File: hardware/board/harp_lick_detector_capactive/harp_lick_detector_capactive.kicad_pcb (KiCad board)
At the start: 4 copper layers, 62.5 x 60.5 mm, 117 parts, among them J1 USB_C_Receptacle_USB2.0, J10 Conn_01x02_Male, J2 Conn_01x03_Male, J3 Conn_01x03_Male, J4 AudioJack3, J5 Barrel_Jack_Switch, J6 Conn_Coaxial, J7 Conn_Coaxial, J8 Conn_Coaxial, J9 Conn_Coaxial, U1 RP2040, U10 LTC6263, U11 CD74AC04, U2 W25Q128JVS, U3 ADUM4160, U4 TPD2EUSB30, U5 LT3030, U6 LM27762, U7 AD9833xRM, U8 LTC6263, U9 LTC6268xS6-10, X1 ECS-TXO-2016, X2 ASE-25.000MHZ-L-C-T

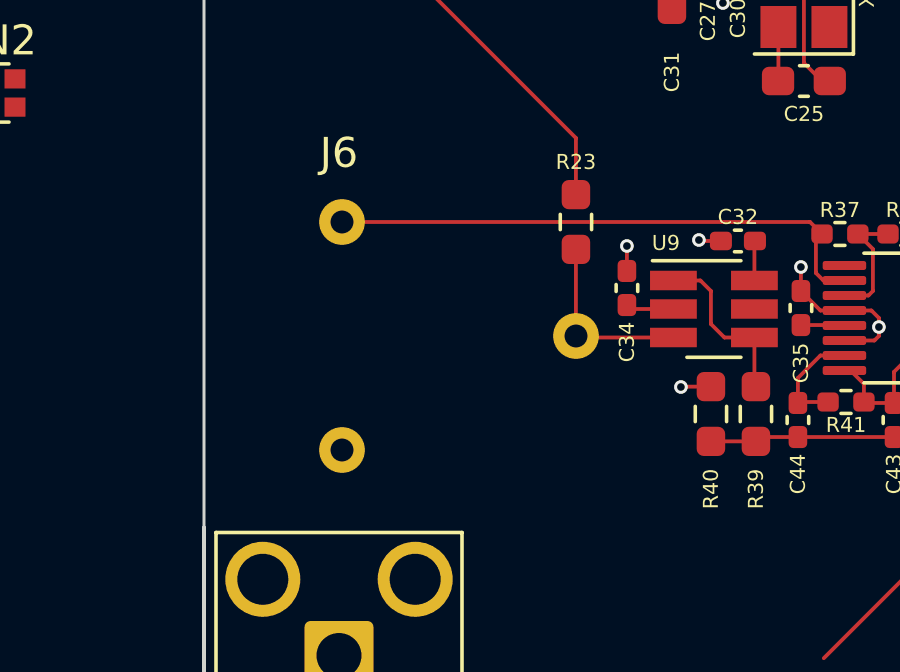
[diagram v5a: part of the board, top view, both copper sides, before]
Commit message: update bandpass filter; plan pico shield version
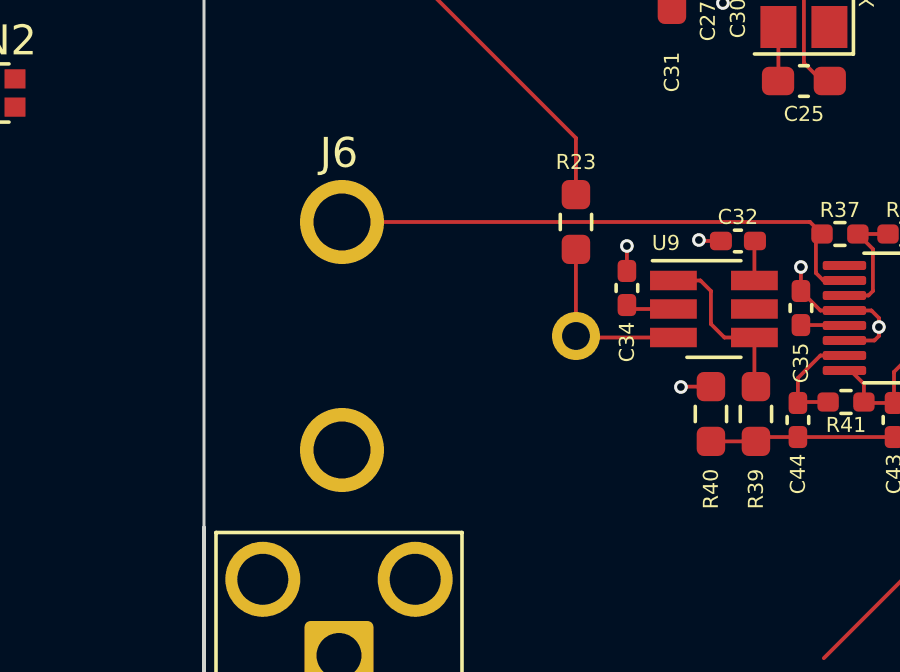
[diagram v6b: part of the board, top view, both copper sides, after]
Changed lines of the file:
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@@
     )
     (fp_line (start -4.825 17.6) (end -4.826 4.6) (layer "Dwgs.User") (width 0.12))
-    (fp_line (start -4.825 17.6) (end 4.825 17.6) (layer "Dwgs.User") (width 0.12))
     (fp_line (start -4.8255 -4.2) (end 4.8255 -4.2) (layer "Dwgs.User") (width 0.12))
     (fp_line (start -4.826 4.6) (end 4.825 4.6) (layer "Dwgs.User") (width 0.12))
+    (fp_line (start -4.825 17.6) (end 4.825 17.6) (layer "Dwgs.User") (width 0.12))
     (fp_line (start 4.825 4.6) (end 4.825 17.6) (layer "Dwgs.User") (width 0.12))
+    (fp_line (start 5.33 -4.69) (end -5.33 -4.69) (layer "F.CrtYd") (width 0.05))
+    (fp_line (start 5.33 5.1) (end 5.33 -4.69) (layer "F.CrtYd") (width 0.05))
     (fp_line (start 5.33 5.1) (end -5.33 5.1) (layer "F.CrtYd") (width 0.05))
-    (fp_line (start 5.33 5.1) (end 5.33 -4.69) (layer "F.CrtYd") (width 0.05))
     (fp_line (start -5.33 5.1) (end -5.33 -4.69) (layer "F.CrtYd") (width 0.05))
-    (fp_line (start 5.33 -4.69) (end -5.33 -4.69) (layer "F.CrtYd") (width 0.05))
-    (pad "1" thru_hole circle (at 0 -7.8 270) (size 1.524 1.524) (drill 0.762) (layers *.Cu *.Mask)
+    (pad "1" thru_hole circle (at 0 -7.8 270) (size 1.6 1.6) (drill 0.93) (layers *.Cu *.Mask)
       (net 41 "Net-(J6-Pad1)") (pinfunction "In") (pintype "passive"))
-    (pad "2" thru_hole circle (at 3.8 0 270) (size 1.524 1.524) (drill 0.762) (layers *.Cu *.Mask)
+    (pad "2" thru_hole circle (at 3.8 0 270) (size 2.8 2.8) (drill 1.9) (layers *.Cu *.Mask)
       (net 42 "Net-(J6-Pad2)") (pinfunction "Ext") (pintype "passive"))
-    (pad "2" thru_hole circle (at -3.8 0 270) (size 1.524 1.524) (drill 0.762) (layers *.Cu *.Mask)
+    (pad "2" thru_hole circle (at -3.8 0 270) (size 2.8 2.8) (drill 1.9) (layers *.Cu *.Mask)
       (net 42 "Net-(J6-Pad2)") (pinfunction "Ext") (pintype "passive"))
   )

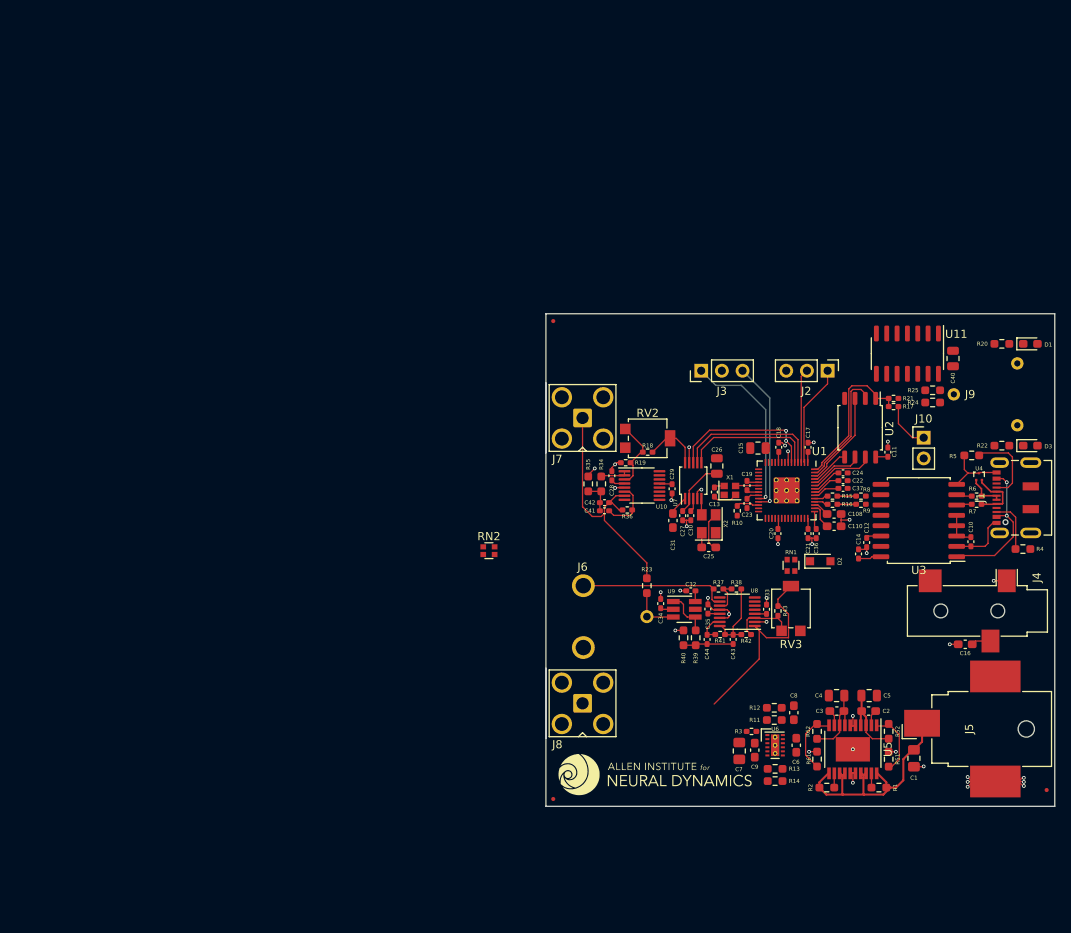
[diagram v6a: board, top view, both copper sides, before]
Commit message: draft ads7029 pio driver
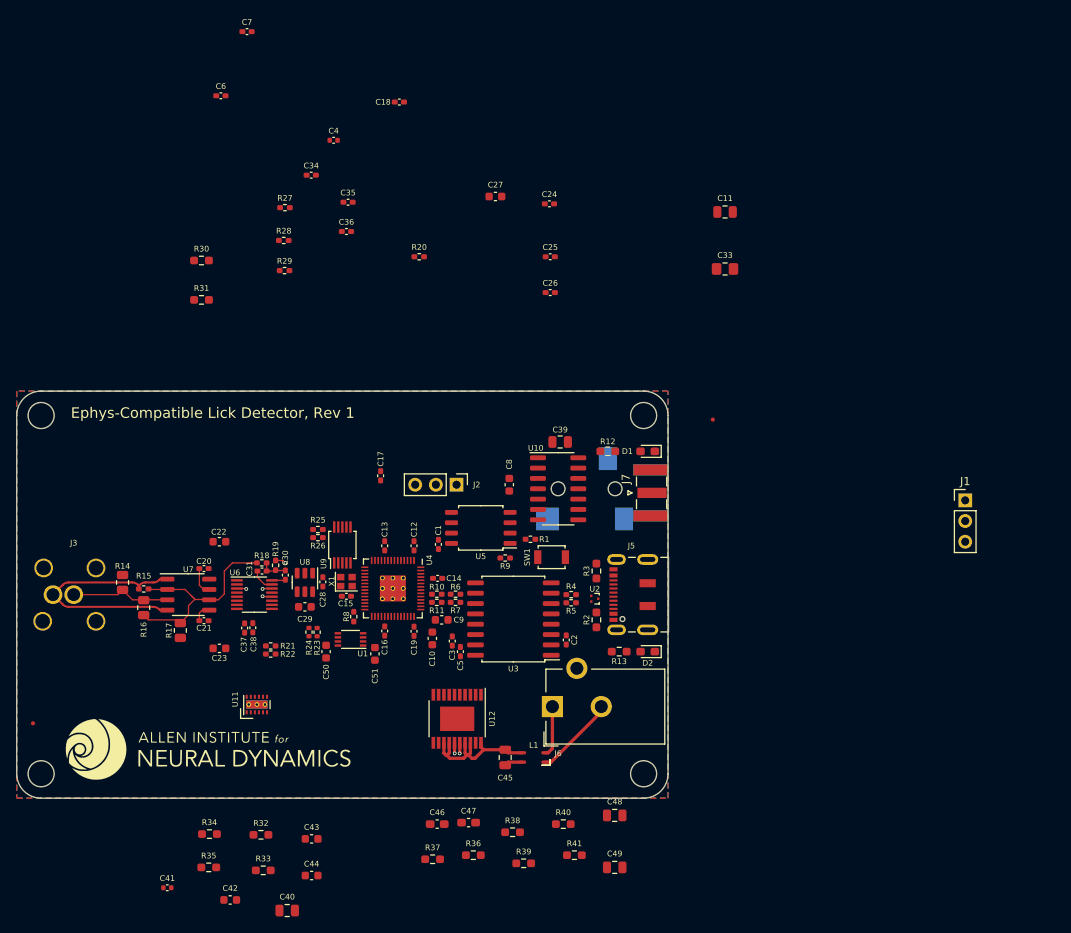
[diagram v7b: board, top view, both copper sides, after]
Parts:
- removed C108, C110: 1uF, Capacitor_SMD:C_0603_1608Metric_Pad1.08x0.95mm_HandSolder
- removed C32: 100nF, Capacitor_SMD:C_0402_1005Metric_Pad0.74x0.62mm_HandSolder
- removed D3: LED, LED_SMD:LED_0603_1608Metric_Pad1.05x0.95mm_HandSolder
- removed the G*** at (183.3, 115.2)
- removed J10: Conn_01x02_Male, Connector_PinHeader_2.54mm:PinHeader_1x02_P2.54mm_Vertical
- removed J8: Conn_Coaxial, Connector_Coaxial:SMA_Amphenol_901-143_Horizontal
- removed J9: Conn_Coaxial, machine_agency_components:conn_bnc_receptacle_50ohm
- removed R42, R43: 390, Resistor_SMD:R_0402_1005Metric_Pad0.72x0.64mm_HandSolder
- removed R51, R61: 100K, Resistor_SMD:R_0603_1608Metric_Pad0.98x0.95mm_HandSolder
- removed R52: 309K, Resistor_SMD:R_0603_1608Metric_Pad0.98x0.95mm_HandSolder
- removed R62: 172K, Resistor_SMD:R_0603_1608Metric_Pad0.98x0.95mm_HandSolder
- removed RN1, RN2: 5K, Resistor_SMD:R_Array_Convex_2x0606
- removed RV2, RV3: R_Potentiometer_Trim, Potentiometer_SMD:Potentiometer_Bourns_3314G_Vertical
- removed X2: ASE-25.000MHZ-L-C-T, Crystal:Crystal_SMD_Abracon_ABM8G-4Pin_3.2x2.5mm
- added C38: 160pF, Capacitor_SMD:C_0402_1005Metric_Pad0.74x0.62mm_HandSolder, F.Cu at (133.9, 97.2)
- added C39: 10uF, Capacitor_SMD:C_0805_2012Metric, F.Cu at (171.7, 74.3)
- added C45: 3.3uF, Capacitor_SMD:C_0805_2012Metric, F.Cu at (164.9, 113.1)
- added C46: 10nF, Capacitor_SMD:C_0603_1608Metric_Pad1.08x0.95mm_HandSolder, F.Cu at (156.5, 121.3)
- added C47: 10nF, Capacitor_SMD:C_0603_1608Metric_Pad1.08x0.95mm_HandSolder, F.Cu at (160.4, 121.1)
- added C48: 10uF, Capacitor_SMD:C_0805_2012Metric, F.Cu at (178.3, 120.2)
- added C49: 22uF, Capacitor_SMD:C_0805_2012Metric, F.Cu at (178.3, 126.6)
- added C50: 2.2uF, Capacitor_SMD:C_0603_1608Metric, F.Cu at (142.9, 100.1)
- added C51: 2.2uF, Capacitor_SMD:C_0603_1608Metric, F.Cu at (148.9, 100.4)
- added G***: LOGO, LOGO, F.Cu at (128.4, 112.1)
- added L1: L_Coupled_1423, kicad_component_library:L_CommonModeChoke_TDKCorporation_1210, F.Cu at (168.4, 113.1)
- added R26: 3K2, Resistor_SMD:R_0402_1005Metric_Pad0.72x0.64mm_HandSolder, F.Cu at (141.9, 86.1)
- added R27: 49K9, Resistor_SMD:R_0402_1005Metric_Pad0.72x0.64mm_HandSolder, F.Cu at (137.8, 45.6)
- added R28: 1K02, Resistor_SMD:R_0402_1005Metric_Pad0.72x0.64mm_HandSolder, F.Cu at (137.7, 49.6)
- added R29: 100K, Resistor_SMD:R_0402_1005Metric_Pad0.72x0.64mm_HandSolder, F.Cu at (137.8, 53.3)
- added R30: 100, Resistor_SMD:R_0603_1608Metric_Pad0.98x0.95mm_HandSolder, F.Cu at (127.6, 52.1)
- added R31: 100, Resistor_SMD:R_0603_1608Metric_Pad0.98x0.95mm_HandSolder, F.Cu at (127.6, 56.9)
- added R32: 54K9, Resistor_SMD:R_0603_1608Metric_Pad0.98x0.95mm_HandSolder, F.Cu at (134.9, 122.6)
- added R33: 53K6, Resistor_SMD:R_0603_1608Metric_Pad0.98x0.95mm_HandSolder, F.Cu at (135.2, 127.0)
- added REF**: MountingHole_3.2mm_M3_DIN965, MountingHole:MountingHole_3.2mm_M3_DIN965, F.Cu at (107.9, 71.1)
- added REF**: MountingHole_3.2mm_M3_DIN965, MountingHole:MountingHole_3.2mm_M3_DIN965, F.Cu at (107.9, 115.1)
- added REF**: MountingHole_3.2mm_M3_DIN965, MountingHole:MountingHole_3.2mm_M3_DIN965, F.Cu at (181.9, 115.1)
- added REF**: MountingHole_3.2mm_M3_DIN965, MountingHole:MountingHole_3.2mm_M3_DIN965, F.Cu at (181.9, 71.1)
- added SW1: SW_Push, Button_Switch_SMD:SW_SPST_B3U-1000P, F.Cu at (170.6, 88.5)
- added U12: LT3030, Package_SO:ETSSOP-20-1EP_4.4x6.5mm_P0.65mm_EP3x4.2mm, F.Cu at (159.0, 108.3)
- C1: value 3.3uF -> 100nF; footprint Capacitor_SMD:C_0805_2012Metric_Pad1.18x1.45mm_HandSolder -> Capacitor_SMD:C_0402_1005Metric_Pad0.74x0.62mm_HandSolder
- C10: value 100nF -> 1uF; footprint Capacitor_SMD:C_0402_1005Metric_Pad0.74x0.62mm_HandSolder -> Capacitor_SMD:C_0603_1608Metric
- C11: value 100nF -> 10uF; footprint Capacitor_SMD:C_0402_1005Metric_Pad0.74x0.62mm_HandSolder -> Capacitor_SMD:C_0805_2012Metric
- C15, C26: value 10uF -> 100nF; footprint Capacitor_SMD:C_0805_2012Metric -> Capacitor_SMD:C_0402_1005Metric_Pad0.74x0.62mm_HandSolder
- C16, C6: value 1uF -> 100nF; footprint Capacitor_SMD:C_0603_1608Metric_Pad1.08x0.95mm_HandSolder -> Capacitor_SMD:C_0402_1005Metric_Pad0.74x0.62mm_HandSolder
- C2, C25, C3: value 10nF -> 100nF; footprint Capacitor_SMD:C_0603_1608Metric_Pad1.08x0.95mm_HandSolder -> Capacitor_SMD:C_0402_1005Metric_Pad0.74x0.62mm_HandSolder
- C22, C23, C27, C29: value 100nF -> 10uF; footprint Capacitor_SMD:C_0402_1005Metric_Pad0.74x0.62mm_HandSolder -> Capacitor_SMD:C_0603_1608Metric
- C30, C37: value 100nF -> 160pF
- C31: value 10nF -> 160pF; footprint Capacitor_SMD:C_0603_1608Metric_Pad1.08x0.95mm_HandSolder -> Capacitor_SMD:C_0402_1005Metric_Pad0.74x0.62mm_HandSolder
- C33: value 100nF -> 10uF; footprint Capacitor_SMD:C_0402_1005Metric_Pad0.74x0.62mm_HandSolder -> Capacitor_SMD:C_0805_2012Metric_Pad1.18x1.45mm_HandSolder
- C36: value 100nF -> 10nF
- C4: value 10uF -> 10nF; footprint Capacitor_SMD:C_0805_2012Metric -> Capacitor_SMD:C_0402_1005Metric
- C40: value 10uF -> 22uF
- C41: value 160pF -> 1uF; footprint Capacitor_SMD:C_0402_1005Metric_Pad0.74x0.62mm_HandSolder -> Capacitor_SMD:C_0402_1005Metric
- C42: value 160pF -> 4.7uF; footprint Capacitor_SMD:C_0402_1005Metric_Pad0.74x0.62mm_HandSolder -> Capacitor_SMD:C_0603_1608Metric
- C43, C44: value 160pF -> 2.2uF; footprint Capacitor_SMD:C_0402_1005Metric_Pad0.74x0.62mm_HandSolder -> Capacitor_SMD:C_0603_1608Metric
- C5: value 22uF -> 100nF; footprint Capacitor_SMD:C_0805_2012Metric -> Capacitor_SMD:C_0402_1005Metric_Pad0.74x0.62mm_HandSolder
- C7: value 4.7uF -> 100nF; footprint Capacitor_SMD:C_0805_2012Metric_Pad1.18x1.45mm_HandSolder -> Capacitor_SMD:C_0402_1005Metric_Pad0.74x0.62mm_HandSolder
- C8, C9: value 2.2uF -> 1uF; footprint Capacitor_SMD:C_0603_1608Metric_Pad1.08x0.95mm_HandSolder -> Capacitor_SMD:C_0603_1608Metric
- D2: value BZX384-A3V3-QX -> LED; footprint Diode_SMD:D_SOD-323_HandSoldering -> LED_SMD:LED_0603_1608Metric_Pad1.05x0.95mm_HandSolder
- J1: value USB_C_Receptacle_USB2.0 -> Conn_01x03_Male; footprint Connector_USB:USB_C_Receptacle_JAE_DX07S016JA1R1500 -> Connector_PinHeader_2.54mm:PinHeader_1x03_P2.54mm_Vertical
- J3: value Conn_01x03_Male -> Conn_Triaxial; footprint Connector_PinHeader_2.54mm:PinHeader_1x03_P2.54mm_Vertical -> kicad_component_library:TRB_Trompeter_CBBJR79A_Horizontal
- J4: moved to B.Cu
- J5: value Barrel_Jack_Switch -> USB_C_Receptacle_USB2.0; footprint Connector_BarrelJack:BarrelJack_CUI_PJ-036AH-SMT_Horizontal -> Connector_USB:USB_C_Receptacle_JAE_DX07S016JA1R1500
- J6: value Conn_Coaxial -> Barrel_Jack_Switch; footprint machine_agency_components:conn_bnc_receptacle_50ohm -> Connector_BarrelJack:BarrelJack_CUI_PJ-102AH_Horizontal
- J7: footprint Connector_Coaxial:SMA_Amphenol_901-143_Horizontal -> Connector_Coaxial:SMA_Samtec_SMA-J-P-X-ST-EM1_EdgeMount
- R1: value 1M -> 1K; footprint Resistor_SMD:R_0603_1608Metric_Pad0.98x0.95mm_HandSolder -> Resistor_SMD:R_0402_1005Metric_Pad0.72x0.64mm_HandSolder
- R10: value 10K -> 27
- R11: value 54K9 -> 27; footprint Resistor_SMD:R_0603_1608Metric_Pad0.98x0.95mm_HandSolder -> Resistor_SMD:R_0402_1005Metric_Pad0.72x0.64mm_HandSolder
- R12: value 51K -> 330
- R13: value 53K6 -> 330
- R14: value 51K -> 100K; footprint Resistor_SMD:R_0603_1608Metric_Pad0.98x0.95mm_HandSolder -> Resistor_SMD:R_0805_2012Metric
- R15: value 27 -> 100
- R16: value 27 -> 100K; footprint Resistor_SMD:R_0402_1005Metric_Pad0.72x0.64mm_HandSolder -> Resistor_SMD:R_0805_2012Metric
- R17: value 1K -> 100K; footprint Resistor_SMD:R_0402_1005Metric_Pad0.72x0.64mm_HandSolder -> Resistor_SMD:R_0805_2012Metric
- R18: value 100K -> 49K9
- R19: value 7.68 -> 1K02
- R2: value 1M -> 5K1
- R20: value 330 -> 100K; footprint Resistor_SMD:R_0603_1608Metric_Pad0.98x0.95mm_HandSolder -> Resistor_SMD:R_0402_1005Metric_Pad0.72x0.64mm_HandSolder
- R21: value 10K -> 68
- R22: value 330 -> 10K; footprint Resistor_SMD:R_0603_1608Metric_Pad0.98x0.95mm_HandSolder -> Resistor_SMD:R_0402_1005Metric_Pad0.72x0.64mm_HandSolder
- R23: value 1M -> 1K; footprint Resistor_SMD:R_0603_1608Metric_Pad0.98x0.95mm_HandSolder -> Resistor_SMD:R_0402_1005Metric
- R24: value 100 -> 1K; footprint Resistor_SMD:R_0603_1608Metric_Pad0.98x0.95mm_HandSolder -> Resistor_SMD:R_0402_1005Metric
- R25: value 100 -> 100K; footprint Resistor_SMD:R_0603_1608Metric_Pad0.98x0.95mm_HandSolder -> Resistor_SMD:R_0402_1005Metric_Pad0.72x0.64mm_HandSolder
- R3: value 10K -> 5K1; footprint Resistor_SMD:R_0402_1005Metric_Pad0.72x0.64mm_HandSolder -> Resistor_SMD:R_0603_1608Metric_Pad0.98x0.95mm_HandSolder
- R34: value 98K8 -> 51K
- R35: value 501 -> 51K
- R36: value 198K -> 1M; footprint Resistor_SMD:R_0402_1005Metric_Pad0.72x0.64mm_HandSolder -> Resistor_SMD:R_0603_1608Metric_Pad0.98x0.95mm_HandSolder
- R37: value 10K -> 1M; footprint Resistor_SMD:R_0402_1005Metric_Pad0.72x0.64mm_HandSolder -> Resistor_SMD:R_0603_1608Metric_Pad0.98x0.95mm_HandSolder
- R38: value 10K -> 309K; footprint Resistor_SMD:R_0402_1005Metric_Pad0.72x0.64mm_HandSolder -> Resistor_SMD:R_0603_1608Metric_Pad0.98x0.95mm_HandSolder
- R39: value 98K8 -> 172K
- R4, R5: value 5K1 -> 24; footprint Resistor_SMD:R_0603_1608Metric_Pad0.98x0.95mm_HandSolder -> Resistor_SMD:R_0402_1005Metric_Pad0.72x0.64mm_HandSolder
- R40: value 501 -> 100K
- R41: value 198K -> 100K; footprint Resistor_SMD:R_0402_1005Metric_Pad0.72x0.64mm_HandSolder -> Resistor_SMD:R_0603_1608Metric_Pad0.98x0.95mm_HandSolder
- R8, R9: value 24 -> 10K
- U1: value RP2040 -> ADS7029; footprint machine_agency_components:RP2040-QFN-56 -> Package_SO:VSSOP-8_2.3x2mm_P0.5mm
- U10: value LTC6263 -> CD74AC04; footprint Package_SO:MSOP-16_3x4mm_P0.5mm -> Package_SO:SOIC-14_3.9x8.7mm_P1.27mm
- U11: value CD74AC04 -> LM27762; footprint Package_SO:SOIC-14_3.9x8.7mm_P1.27mm -> Package_SON:WSON-12-1EP_3x2mm_P0.5mm_EP1x2.65_ThermalVias
- U2: value W25Q128JVS -> TPD2EUSB30; footprint Package_SO:SOIC-8_5.23x5.23mm_P1.27mm -> Package_TO_SOT_SMD:Texas_DRT-3
- U4: value TPD2EUSB30 -> RP2040; footprint Package_TO_SOT_SMD:Texas_DRT-3 -> kicad_component_library:RP2040-QFN-56
- U5: value LT3030 -> W25Q128JVS; footprint Package_SO:ETSSOP-20-1EP_4.4x6.5mm_P0.65mm_EP3x4.2mm -> Package_SO:SOIC-8_5.23x5.23mm_P1.27mm
- U6: value LM27762 -> LTC6263; footprint Package_SON:WSON-12-1EP_3x2mm_P0.5mm_EP1x2.65_ThermalVias -> Package_SO:MSOP-16_3x4mm_P0.5mm
- U7: value AD9833xRM -> LTC6268xS8-10; footprint Package_SO:MSOP-10_3x3mm_P0.5mm -> Package_SO:SO-8_3.9x4.9mm_P1.27mm
- U8: value LTC6263 -> REF3433QDBVRQ1; footprint Package_SO:MSOP-16_3x4mm_P0.5mm -> Package_TO_SOT_SMD:SOT-23-6
- U9: value LTC6268xS6-10 -> AD9833xRM; footprint Package_TO_SOT_SMD:SOT-23-6_Handsoldering -> Package_SO:MSOP-10_3x3mm_P0.5mm
- moved FID1 124.8 mm to (106.9, 108.9)
- moved C7 107.1 mm to (133.2, 23.9), turned to 0 degrees
- moved C6 106.6 mm to (130.0, 31.8), turned to 0 degrees
- moved C40 106.2 mm to (138.1, 131.9), turned to 0 degrees
- moved R22 93.4 mm to (136.1, 100.4), turned to 0 degrees
- moved C4 92.0 mm to (143.8, 37.3), turned to 0 degrees
- moved R17 91.8 mm to (125.0, 97.5), turned to -90 degrees
- moved U11 90.8 mm to (134.4, 106.6), turned to 90 degrees
- moved R16 85.5 mm to (120.5, 94.7), turned to -90 degrees
- moved R15 85.4 mm to (120.5, 92.4)
- moved R14 83.8 mm to (117.9, 91.6), turned to -90 degrees
- moved R21 82.3 mm to (136.1, 99.4), turned to 180 degrees
- moved J3 81.8 mm to (111.9, 93.1)
- moved R24 81.6 mm to (140.8, 97.7), turned to -90 degrees
- moved R25 77.4 mm to (141.9, 85.1)
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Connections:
- C1 pad 1: +12V -> GND
- C1 pad 2: GND -> +3V3
- C10 pad 1: GND1 -> +3V3
- C10 pad 2: /MCU/VDD1 -> GND
- C11 pad 1: GND -> +3V3
- C11 pad 2: +3V3 -> GND
- C15 pad 1: +3V3 -> GND
- C15 pad 2: GND -> +3V3
- C16 pad 1: +3V3 -> GND
- C16 pad 2: GND -> +3V3
- C2 pad 1: Net-(C2-Pad1) -> GND1
- C2 pad 2: +5V -> /Harp Core RP2040 + Isolated USB/VDD1
- C20 pad 2: +3V3 -> +2V5
- C21 pad 1: GND -> -2V5
- C21 pad 2: +3V3 -> GND
- C22 pad 2: +3V3 -> +2V5
- C23 pad 1: GND -> -2V5
- C23 pad 2: +1V1 -> GND
- C24 pad 2: +1V1 -> +2V5
- C25 pad 1: GND -> -2V5
- C25 pad 2: +3V3 -> GND
- C26 pad 2: +3V3 -> +5V
- C27 pad 2: +3V3 -> +5V
- C28 pad 1: +2V5 -> GND
- C28 pad 2: GND -> VREF_3V3
- C29 pad 2: -2V5 -> VREF_3V3
- C3 pad 1: Net-(C3-Pad1) -> GND
- C30 pad 1: GND -> Net-(C30-Pad1)
- C31 pad 1: Net-(C31-Pad1) -> Net-(C30-Pad1)
- C31 pad 2: +3V3 -> Net-(U6D--)
- C33 pad 1: GND -> +3V3
- C33 pad 2: +2V5 -> GND
- C34 pad 1: -2V5 -> GND
- C34 pad 2: GND -> +3V3
- C35 pad 1: -2V5 -> GND
- C35 pad 2: GND -> Net-(U9-CAP/2.5V)
- C36 pad 1: GND -> Net-(U9-COMP)
- C37 pad 1: GND -> Net-(C37-Pad1)
- C37 pad 2: +3V3 -> /100KHz Sine Wave/VSINE
- C4 pad 1: +3V3 -> GND
- C4 pad 2: GND -> +3V3
- C41 pad 1: Net-(C41-Pad1) -> Net-(U11-C+)
- C41 pad 2: Net-(C41-Pad2) -> Net-(U11-C-)
- C42 pad 1: Net-(C41-Pad1) -> Net-(U11-CP)
- C42 pad 2: /100[Khz], 50[uVpp] Sine Wave/VSIN -> GND
- C43 pad 1: Net-(C43-Pad1) -> +2V5
- C43 pad 2: Net-(C43-Pad2) -> GND
- C44 pad 1: Net-(C43-Pad1) -> -2V5
- C44 pad 2: Net-(C44-Pad2) -> GND
- C5 pad 1: +5V -> GND
- C5 pad 2: GND -> +3V3
- C6 pad 1: Net-(C6-Pad1) -> GND
- C6 pad 2: Net-(C6-Pad2) -> +1V1
- C7 pad 1: Net-(C7-Pad1) -> GND
- C7 pad 2: GND -> +1V1
- C8 pad 1: +2V5 -> +3V3
- C9 pad 1: -2V5 -> +1V1
- D1 pad 1: Net-(D1-Pad1) -> GND
- D1 pad 2: Net-(D1-Pad2) -> Net-(D1-A)
- D2 pad 1: /MCU/ADC -> GND
- D2 pad 2: GND -> Net-(D2-A)
- J2 pad 1: /MCU/UART0_TXD -> /Harp Core RP2040 + Isolated USB/UART0_TXD
- J2 pad 2: /MCU/UART0_RXD -> /Harp Core RP2040 + Isolated USB/UART0_RXD
- J3 pad 1: /MCU/SWCLK -> /Lick Detection Analog Front End/triax_core
- J3 pad 2: GND -> /Lick Detection Analog Front End/triax_inner_shield
- J3 pad 3: /MCU/SWDIO -> GND
- J4 pad T: /MCU/HARP_CLK_SYNC -> /Harp Core RP2040 + Isolated USB/HARP_CLK_SYNC
- J6 pad 1: Net-(J6-Pad1) -> +12V
- J6 pad 2: Net-(J6-Pad2) -> GND2
- J7 pad 1: /100[Khz], 50[uVpp] Sine Wave/VSIN -> Net-(J7-In)
- R1 pad 1: +12V -> /Harp Core RP2040 + Isolated USB/USB_Boot
- R1 pad 2: Net-(R1-Pad2) -> /Harp Core RP2040 + Isolated USB/QSPI_CS
- R10 pad 1: +3V3 -> Net-(U4-USB_DP)
- R10 pad 2: Net-(R10-Pad2) -> /Harp Core RP2040 + Isolated USB/DD+
- R11 pad 1: +2V5 -> Net-(U4-USB_DM)
- R11 pad 2: Net-(R11-Pad2) -> /Harp Core RP2040 + Isolated USB/DD-
- R12 pad 1: Net-(R11-Pad2) -> Net-(U4-GPIO24)
- R12 pad 2: GND -> Net-(D1-A)
- R13 pad 1: -2V5 -> Net-(U4-GPIO25)
- R13 pad 2: Net-(R13-Pad2) -> Net-(D2-A)
- R14 pad 1: Net-(R13-Pad2) -> /100KHz Sine Wave/VSINE
- R14 pad 2: GND -> /Lick Detection Analog Front End/triax_core
- R15 pad 1: Net-(R15-Pad1) -> /Lick Detection Analog Front End/triax_inner_shield
- R15 pad 2: /MCU/DD+ -> Net-(U7--)
- R16 pad 1: Net-(R16-Pad1) -> /Lick Detection Analog Front End/triax_core
- R16 pad 2: /MCU/DD- -> Net-(U7--)
- R17 pad 1: /MCU/USB_Boot -> Net-(U7--)
- R17 pad 2: /MCU/QSPI_CS -> GND
- R18 pad 1: Net-(R18-Pad1) -> Net-(U7--)
- R18 pad 2: Net-(R18-Pad2) -> Net-(C30-Pad1)
- R19 pad 1: Net-(R18-Pad2) -> GND
- R19 pad 2: GND -> Net-(C30-Pad1)
- R2 pad 1: +12V -> Net-(J5-CC1)
- R2 pad 2: Net-(R2-Pad2) -> GND1
- R20 pad 1: Net-(D1-Pad1) -> Net-(U6D--)
- R20 pad 2: GND -> Net-(C30-Pad2)
- R21 pad 1: /MCU/QSPI_CS -> Net-(C30-Pad2)
- R21 pad 2: +3V3 -> Net-(U6A--)
- R22 pad 1: Net-(D3-Pad1) -> Net-(U6A--)
- R22 pad 2: GND -> Net-(R22-Pad2)
- R23 pad 1: /100[Khz], 50[uVpp] Sine Wave/VSIN -> Net-(U1-AINP)
- R23 pad 2: Net-(J6-Pad1) -> VREF_3V3
- R24 pad 1: Net-(R24-Pad1) -> Net-(R22-Pad2)
- R24 pad 2: Net-(J9-Pad1) -> Net-(U1-AINP)
- R25 pad 1: Net-(R24-Pad1) -> Net-(U6B-+)
- R25 pad 2: Net-(J9-Pad1) -> Net-(U9-VOUT)
- R3 pad 1: +5V -> Net-(J5-CC2)
- R3 pad 2: Net-(R3-Pad2) -> GND1
- R34 pad 1: Net-(R34-Pad1) -> Net-(U11-FB+)
- R34 pad 2: Net-(C41-Pad1) -> GND
- R35 pad 1: GND -> Net-(U11-FB-)
- R35 pad 2: Net-(C41-Pad1) -> GND
- R36 pad 1: Net-(C41-Pad2) -> IN1
- R36 pad 2: /100[Khz], 50[uVpp] Sine Wave/VSIN -> Net-(U12-PWRGD1)
- R37 pad 1: Net-(R37-Pad1) -> IN1
- R37 pad 2: Net-(J6-Pad2) -> Net-(U12-PWRGD2)
- R38 pad 1: Net-(R37-Pad1) -> +5V
- R38 pad 2: Net-(C43-Pad2) -> Net-(U12-ADJ1)
- R39 pad 1: Net-(R39-Pad1) -> +3V3
- R39 pad 2: Net-(C43-Pad1) -> Net-(U12-ADJ2)
- R4 pad 1: Net-(J1-PadA5) -> /Harp Core RP2040 + Isolated USB/D+
- R4 pad 2: GND1 -> Net-(U3-UD+)
- R40 pad 1: GND -> Net-(U12-ADJ1)
- R40 pad 2: Net-(C43-Pad1) -> GND
- R41 pad 1: Net-(C44-Pad2) -> Net-(U12-ADJ2)
- R41 pad 2: Net-(C43-Pad2) -> GND
- R5 pad 1: Net-(J1-PadB5) -> /Harp Core RP2040 + Isolated USB/D-
- R5 pad 2: GND1 -> Net-(U3-UD-)
- R6 pad 1: /MCU/D+ -> Net-(U3-DD+)
- R6 pad 2: Net-(R6-Pad2) -> /Harp Core RP2040 + Isolated USB/DD+
- R7 pad 1: /MCU/D- -> Net-(U3-DD-)
- R7 pad 2: Net-(R7-Pad2) -> /Harp Core RP2040 + Isolated USB/DD-
- R8 pad 1: Net-(R8-Pad1) -> +3V3
- R8 pad 2: /MCU/DD+ -> Net-(U4-RUN)
- R9 pad 1: Net-(R9-Pad1) -> /Harp Core RP2040 + Isolated USB/QSPI_CS
- R9 pad 2: /MCU/DD- -> +3V3
- U1 pad 2: /MCU/UART0_TXD -> /Harp Core RP2040 + Isolated USB/PIO_SCK
- U1 pad 3: /MCU/UART0_RXD -> /Harp Core RP2040 + Isolated USB/PIO_POCI
- U1 pad 4: /SCK -> /Harp Core RP2040 + Isolated USB/PIO_CS
- U1 pad 5: /PICO -> GND
- U1 pad 6: /CS -> Net-(U1-AINP)
- U1 pad 7: /MCU/HARP_CLK_SYNC -> VREF_3V3
- U1 pad 8: unconnected-(U1-Pad8) -> GND
- U10 pad 1: Net-(R34-Pad1) -> unconnected-(U10-Pad1)
- U10 pad 10: unconnected-(U10-Pad10) -> Net-(R30-Pad1)
- U10 pad 11: unconnected-(U10-Pad11) -> Net-(U10-Pad11)
- U10 pad 12: unconnected-(U10-Pad12) -> Net-(R30-Pad1)
- U10 pad 13: -2V5 -> Net-(U10-Pad11)
- U10 pad 14: unconnected-(U10-Pad14) -> +5V
- U10 pad 2: Net-(R34-Pad1) -> unconnected-(U10-Pad2)
- U10 pad 3: Net-(R18-Pad2) -> /Harp Core RP2040 + Isolated USB/TTL_OUT
- U10 pad 4: +2V5 -> Net-(U10-Pad11)
- U10 pad 5: GND -> unconnected-(U10-Pad5)
- U10 pad 6: Net-(C41-Pad2) -> unconnected-(U10-Pad6)
- U10 pad 7: /100[Khz], 50[uVpp] Sine Wave/VSIN -> GND
- U10 pad 8: unconnected-(U10-Pad8) -> Net-(R30-Pad1)
- U10 pad 9: unconnected-(U10-Pad9) -> Net-(U10-Pad11)
- U11 pad 1: unconnected-(U11-Pad1) -> GND
- U11 pad 10: Net-(R24-Pad1) -> Net-(U11-C+)
- U11 pad 11: Net-(U11-Pad11) -> +2V5
- U11 pad 12: Net-(R24-Pad1) -> +5V
- U11 pad 13: Net-(U11-Pad11) -> GND
- U11 pad 2: unconnected-(U11-Pad2) -> Net-(U11-FB+)
- U11 pad 3: /MCU/LICK -> +5V
- U11 pad 4: Net-(U11-Pad11) -> GND
- U11 pad 5: unconnected-(U11-Pad5) -> Net-(U11-CP)
- U11 pad 6: unconnected-(U11-Pad6) -> -2V5
- U11 pad 7: GND -> Net-(U11-FB-)
- U11 pad 8: Net-(R24-Pad1) -> +5V
- U11 pad 9: Net-(U11-Pad11) -> Net-(U11-C-)
- U2 pad 1: /MCU/QSPI_CS -> /Harp Core RP2040 + Isolated USB/D+
- U2 pad 2: /MCU/QSPI_D1 -> /Harp Core RP2040 + Isolated USB/D-
- U2 pad 3: /MCU/QSPI_D2 -> GND1
- U3 pad 10: Net-(R8-Pad1) -> Net-(U3-DD+)
- U3 pad 11: Net-(R9-Pad1) -> Net-(U3-DD-)
- U3 pad 3: /MCU/VDD1 -> /Harp Core RP2040 + Isolated USB/VDD1
- U3 pad 4: /MCU/VDD1 -> /Harp Core RP2040 + Isolated USB/VDD1
- U3 pad 5: /MCU/VDD1 -> /Harp Core RP2040 + Isolated USB/VDD1
- U3 pad 6: Net-(R7-Pad2) -> Net-(U3-UD-)
- U3 pad 7: Net-(R6-Pad2) -> Net-(U3-UD+)
- U4 pad 1: /MCU/D+ -> +3V3
- U4 pad 2: /MCU/D- -> /Harp Core RP2040 + Isolated USB/UART0_TXD
- U4 pad 3: GND1 -> /Harp Core RP2040 + Isolated USB/UART0_RXD
- U5 pad 1: Net-(R51-Pad1) -> /Harp Core RP2040 + Isolated USB/QSPI_CS
- U5 pad 2: Net-(C2-Pad1) -> /Harp Core RP2040 + Isolated USB/QSPI_D1
- U5 pad 3: +5V -> /Harp Core RP2040 + Isolated USB/QSPI_D2
- U5 pad 4: +5V -> GND
- U5 pad 5: GND -> /Harp Core RP2040 + Isolated USB/QSPI_D0
- U5 pad 6: GND -> /Harp Core RP2040 + Isolated USB/QSPI_CLK
- U5 pad 7: +3V3 -> /Harp Core RP2040 + Isolated USB/QSPI_D3
- U6 pad 1: Net-(R3-Pad2) -> Net-(R22-Pad2)
- U6 pad 10: Net-(C6-Pad1) -> /100KHz Sine Wave/VSINE
- U6 pad 11: +2V5 -> Net-(U6C--)
- U6 pad 12: +5V -> GND
- U6 pad 13: GND -> -2V5
- U6 pad 2: Net-(R11-Pad2) -> Net-(U6A--)
- U6 pad 3: +5V -> GND
- U6 pad 4: GND -> +2V5
- U6 pad 5: Net-(C7-Pad1) -> Net-(U6B-+)
- U6 pad 6: -2V5 -> Net-(U6B--)
- U6 pad 7: Net-(R13-Pad2) -> Net-(U6B--)
- U6 pad 8: +5V -> unconnected-(U6E-NC-Pad8)
- U6 pad 9: Net-(C6-Pad2) -> unconnected-(U6E-NC-Pad9)
- U7 pad 1: Net-(C31-Pad1) -> /Lick Detection Analog Front End/triax_inner_shield
- U7 pad 2: +3V3 -> Net-(U7--)
- U7 pad 3: Net-(C30-Pad2) -> /Lick Detection Analog Front End/triax_core
- U7 pad 4: GND -> /Lick Detection Analog Front End/triax_inner_shield
- U7 pad 5: Net-(U7-Pad5) -> -2V5
- U7 pad 6: /PICO -> Net-(U7--)
- U7 pad 7: /SCK -> +2V5
- U7 pad 8: /CS -> unconnected-(U7-~{SHDN}-Pad8)
- U8 pad 1: Net-(J8-Pad1) -> GND
- U8 pad 3: Net-(R42-Pad2) -> +5V
- U8 pad 4: +2V5 -> +5V
- U8 pad 5: unconnected-(U8-Pad5) -> VREF_3V3
- U8 pad 6: unconnected-(U8-Pad6) -> VREF_3V3
- U9 pad 1: Net-(R39-Pad1) -> Net-(U9-COMP)
- U9 pad 2: -2V5 -> +3V3
- U9 pad 3: Net-(J6-Pad1) -> Net-(U9-CAP/2.5V)
- U9 pad 4: Net-(R39-Pad1) -> GND
- U9 pad 5: unconnected-(U9-Pad5) -> /100KHz Sine Wave/xtal_out
- U9 pad 6: +2V5 -> /100KHz Sine Wave/PICO
- X1 pad 3: Net-(U1-Pad20) -> /100KHz Sine Wave/xtal_out
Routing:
- net GND: track 67.8 -> 9.71 mm, vias 35 -> 6
- net +3V3: track 47.8 -> 0.00 mm
- net /Lick Detection Analog Front End/triax_inner_shield: track 0.00 -> 30.1 mm
- net /100[Khz], 50[uVpp] Sine Wave/VSIN: track 29.9 -> 0.00 mm
- net Net-(U7--): track 0.00 -> 26.6 mm
- net +12V: track 32.4 -> 6.27 mm
- net Net-(J8-Pad1): track 24.8 -> 0.00 mm
- net /MCU/SWCLK: track 21.6 -> 0.00 mm, vias 1 -> 0
- net /MCU/QSPI_CS: track 18.8 -> 0.00 mm
- net /MCU/SWDIO: track 18.8 -> 0.00 mm, vias 1 -> 0
- net Net-(J6-Pad2): track 18.6 -> 0.00 mm
- net /CS: track 18.4 -> 0.00 mm, vias 2 -> 0
- net IN1: track 0.00 -> 18.0 mm
- net /SCK: track 17.9 -> 0.00 mm
- net VBUS: track 17.7 -> 0.00 mm, vias 2 -> 0
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- added copper zone on B.Cu, net GND
- added copper zone on F.Cu, net GND
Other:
- board size 62.5 x 60.5 mm -> 80 x 50 mm
- board text added: "Ephys-Compatible Lick Detector, Rev 1"
- board text added: "FIXME: add ground terminal Lug."
- board text added: "FIXME: add more test points. * Signals * Power Supplies"
- board text added: "FIXME: change SMA connector to right angle SMD. (Needs more vertical space from headphone jack.)"
- board text added: "Fits in enclosure: 1457C801E or 1457C801EBK"
- board text added: "Setup Notes: * The ground lug must be connected to the chassis ground of the rig. * The USB port is magnetically coupled but not electrically connected to the PC. * USB and 3.5mm (Harp) connections are not needed if solely using the TTL output."
- board text added: "Vasquez"
- board text added: "https://github.com/AllenNeuralDynamics/harp.device.lick-detector"
- board text removed: "TODO: Consider top mounting SMA connectors that can be hidden/DNPed in the final design."
- board text removed: "TODO: add the RP2040 package"
- board text removed: "TODO: move TVS diode in-between D+/D- pair"

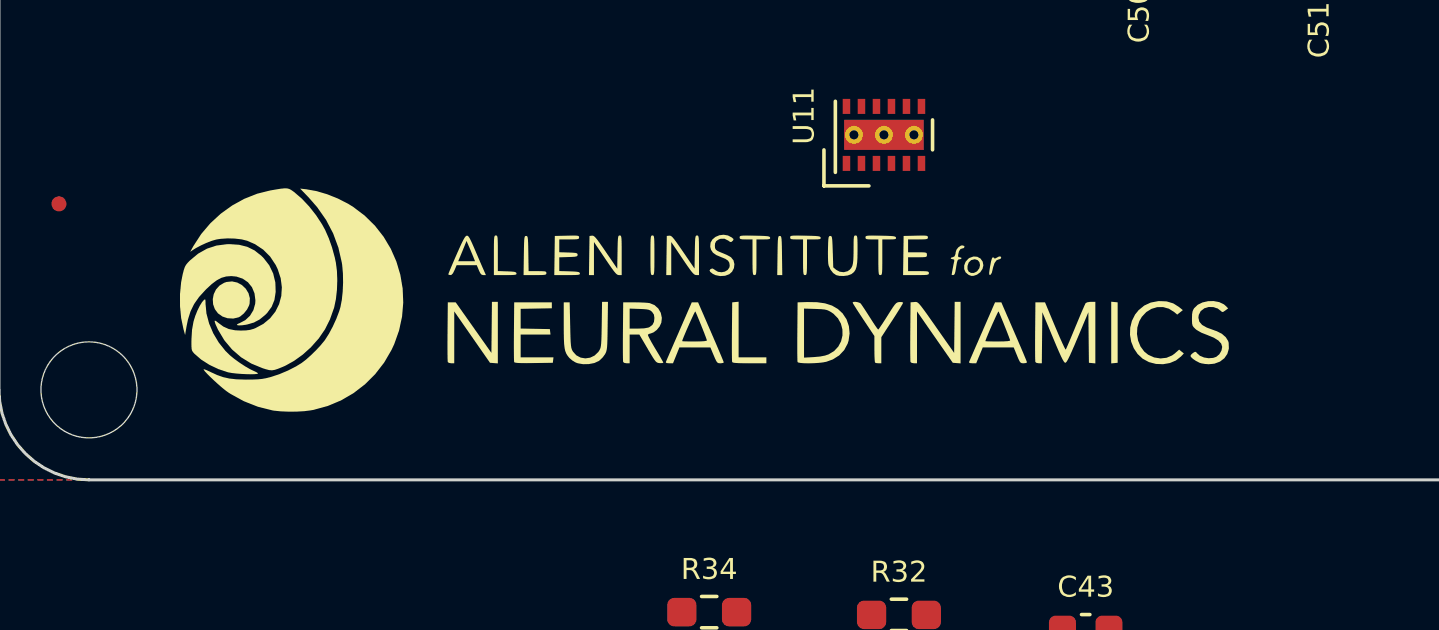
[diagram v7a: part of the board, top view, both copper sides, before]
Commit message: draft pio ads70x9 class; compiles
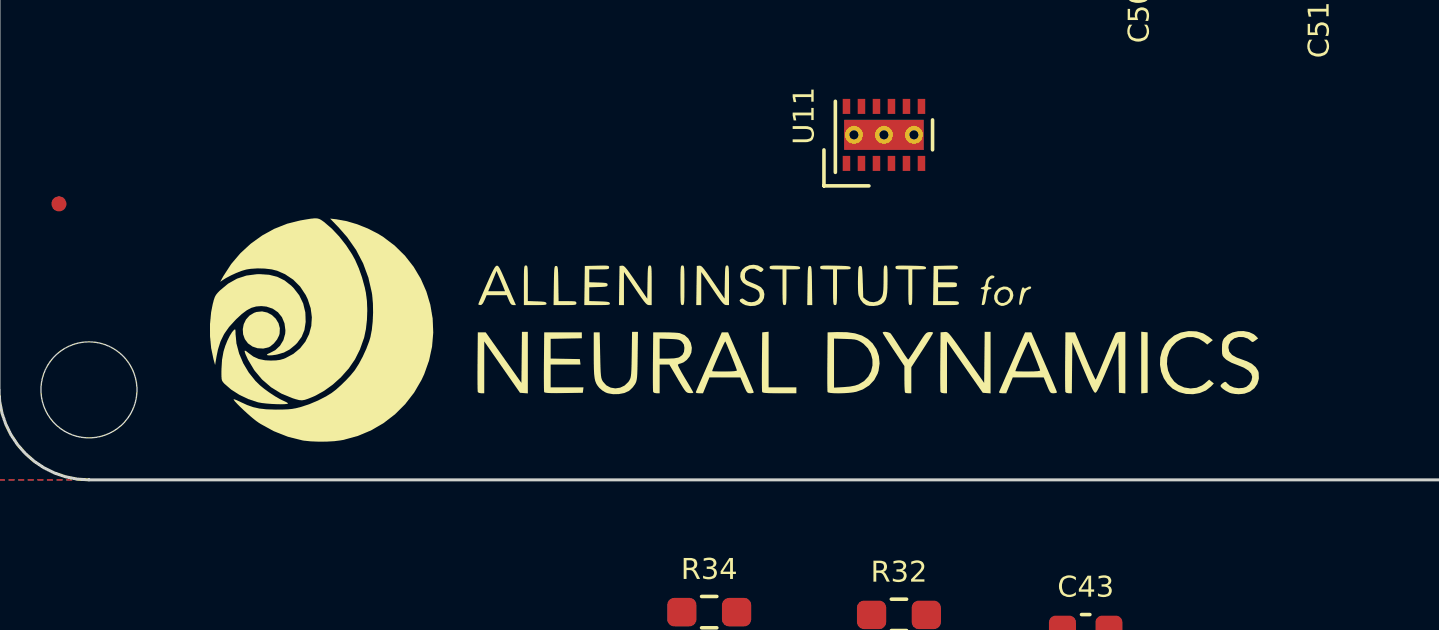
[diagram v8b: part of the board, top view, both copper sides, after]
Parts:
- moved G*** 1.41 mm to (129.4, 113.1)
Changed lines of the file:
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@@
   )
   (footprint "LOGO" (layer "F.Cu")
-    (at 128.4 112.1)
+    (at 129.4 113.1)
     (attr board_only exclude_from_pos_files exclude_from_bom)
     (fp_text reference "G***" (at 0 0) (layer "F.SilkS") hide
